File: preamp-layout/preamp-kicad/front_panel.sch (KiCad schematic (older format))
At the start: 11 parts

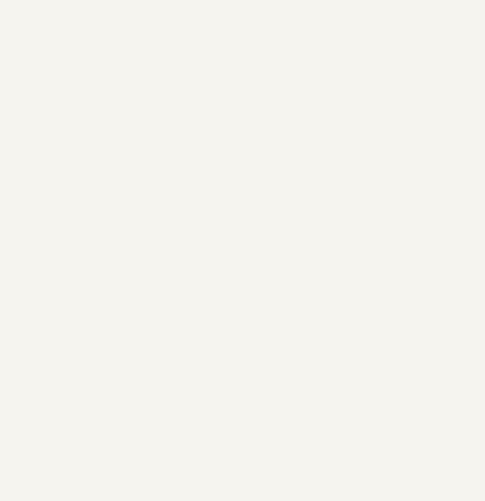
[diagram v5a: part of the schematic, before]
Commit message: Updates
Minor Readme updates.
Schematic:
 - Bus connector lines replaced single wire connectors
 - Title block populated.
 - Power Supply updates.
 - Preliminary Front Panel.
 - Minor MCU work.
 -
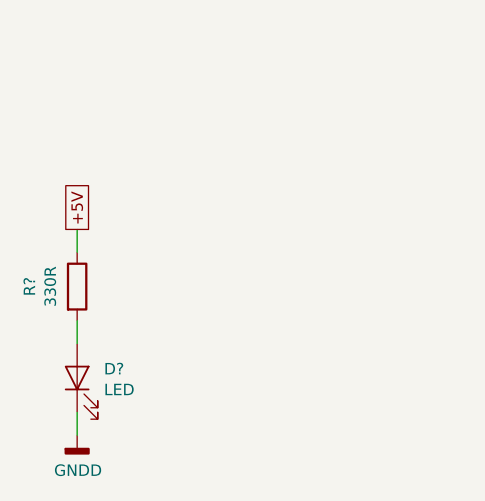
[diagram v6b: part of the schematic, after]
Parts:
- added D?: LED, symbol Device:LED
- added R?: 330R, symbol Device:R
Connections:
- net +5V: now also R?.1
- net GNDD: now also D?.1 (K)
- new net: D?.2 (A), R?.2
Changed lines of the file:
@@
 $Descr A4 11693 8268
 encoding utf-8
-Sheet 9 13
-Title ""
-Date ""
-Rev ""
+Sheet 7 13
+Title "Front Panel"
+Date "2020-01-09"
+Rev "A00"
 Comp ""
-Comment1 ""
-Comment2 ""
-Comment3 ""
-Comment4 ""
+Comment1 "creativecommons.org/licenses/by/4.0/"
+Comment2 "License: CC BY 4.0"
+Comment3 "github.com/SlurpyTurts/preamp"
+Comment4 "Author: Jordon Gerber"
 $EndDescr
 Text GLabel 5150 2250 1    50   UnSpc ~ 0
@@
 Wire Wire Line
 	1700 2100 1800 2100
+Text GLabel 1250 6200 1    50   UnSpc ~ 0
++5V
+$Comp
+L power:GNDD #PWR?
+U 1 1 5FF4C386
+P 1250 7100
+AR Path="/5E2D8DA2/5FF4C386" Ref="#PWR?"  Part="1"
+AR Path="/5E5ECAAE/5FF4C386" Ref="#PWR?"  Part="1"
+F 0 "#PWR?" H 1250 6850 50  0001 C CNN
+F 1 "GNDD" H 1254 6945 50  0000 C CNN
+F 2 "" H 1250 7100 50  0001 C CNN
+F 3 "" H 1250 7100 50  0001 C CNN
+	1    1250 7100
+	1    0    0    -1
+$EndComp
+$Comp
+L Device:R R?
+U 1 1 5FF4C38C
+P 1250 6450
+AR Path="/5E2D8DA2/5FF4C38C" Ref="R?"  Part="1"
+AR Path="/5FF4C38C" Ref="R?"  Part="1"
+AR Path="/5E5ECAAE/5FF4C38C" Ref="R?"  Part="1"
+F 0 "R?" V 1043 6450 50  0000 C CNN
+F 1 "330R" V 1134 6450 50  0000 C CNN
+F 2 "" V 1180 6450 50  0001 C CNN
+F 3 "~" H 1250 6450 50  0001 C CNN
+	1    1250 6450
+	1    0    0    -1
+$EndComp
+$Comp
+L Device:LED D?
+U 1 1 5FF4C392
+P 1250 6850
+AR Path="/5E2D8DA2/5FF4C392" Ref="D?"  Part="1"
+AR Path="/5E5ECAAE/5FF4C392" Ref="D?"  Part="1"
+F 0 "D?" V 1289 6733 50  0000 R CNN
+F 1 "LED" V 1198 6733 50  0000 R CNN
+F 2 "" H 1250 6850 50  0001 C CNN
+F 3 "~" H 1250 6850 50  0001 C CNN
+	1    1250 6850
+	0    -1   -1   0
+$EndComp
+Wire Wire Line
+	1250 6200 1250 6300
+Wire Wire Line
+	1250 6600 1250 6700
+Wire Wire Line
+	1250 7000 1250 7100
 $EndSCHEMATC

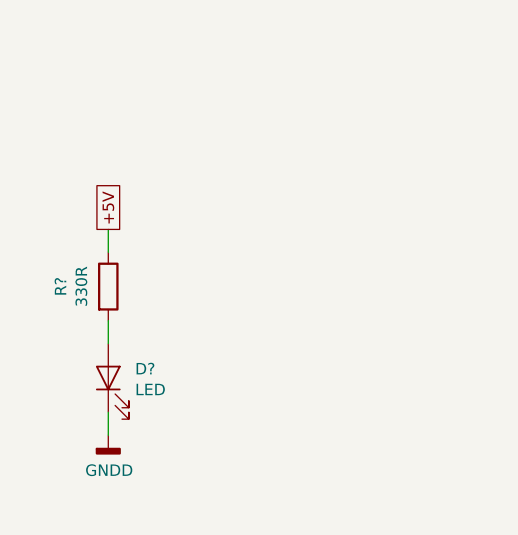
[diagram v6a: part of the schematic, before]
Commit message: Power conn cleanup
5V and 15V cleaned up on all sheets
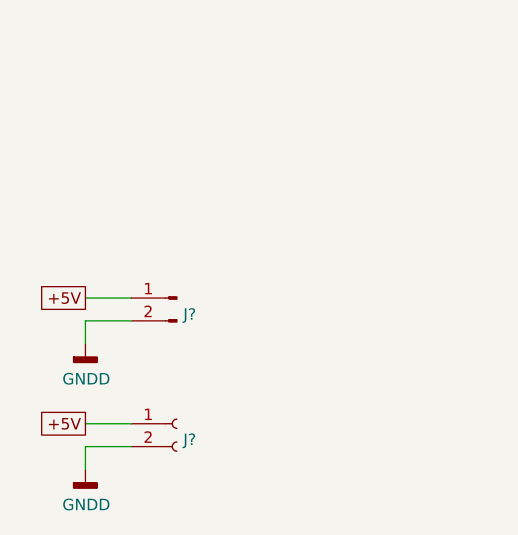
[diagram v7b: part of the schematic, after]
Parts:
- removed D?: LED, symbol Device:LED
- removed R?: 330R, symbol Device:R
- added J?: Conn_01x02_Male, symbol Connector:Conn_01x02_Male
- added J?: Conn_01x02_Female, symbol Connector:Conn_01x02_Female
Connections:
- net +5V: now also J?.1 (Pin_1), J?.1 (Pin_1)
- net GNDD: now also J?.2 (Pin_2), J?.2 (Pin_2)
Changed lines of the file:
@@
 $Descr A4 11693 8268
 encoding utf-8
-Sheet 7 13
+Sheet 6 13
 Title "Front Panel"
 Date "2020-01-09"
@@
 Wire Wire Line
 	1700 2100 1800 2100
-Text GLabel 1250 6200 1    50   UnSpc ~ 0
-+5V
-$Comp
-L power:GNDD #PWR?
-U 1 1 5FF4C386
-P 1250 7100
-AR Path="/5E2D8DA2/5FF4C386" Ref="#PWR?"  Part="1"
-AR Path="/5E5ECAAE/5FF4C386" Ref="#PWR?"  Part="1"
-F 0 "#PWR?" H 1250 6850 50  0001 C CNN
-F 1 "GNDD" H 1254 6945 50  0000 C CNN
-F 2 "" H 1250 7100 50  0001 C CNN
-F 3 "" H 1250 7100 50  0001 C CNN
-	1    1250 7100
-	1    0    0    -1
-$EndComp
-$Comp
-L Device:R R?
-U 1 1 5FF4C38C
-P 1250 6450
-AR Path="/5E2D8DA2/5FF4C38C" Ref="R?"  Part="1"
-AR Path="/5FF4C38C" Ref="R?"  Part="1"
-AR Path="/5E5ECAAE/5FF4C38C" Ref="R?"  Part="1"
-F 0 "R?" V 1043 6450 50  0000 C CNN
-F 1 "330R" V 1134 6450 50  0000 C CNN
-F 2 "" V 1180 6450 50  0001 C CNN
-F 3 "~" H 1250 6450 50  0001 C CNN
-	1    1250 6450
-	1    0    0    -1
-$EndComp
-$Comp
-L Device:LED D?
-U 1 1 5FF4C392
-P 1250 6850
-AR Path="/5E2D8DA2/5FF4C392" Ref="D?"  Part="1"
-AR Path="/5E5ECAAE/5FF4C392" Ref="D?"  Part="1"
-F 0 "D?" V 1289 6733 50  0000 R CNN
-F 1 "LED" V 1198 6733 50  0000 R CNN
-F 2 "" H 1250 6850 50  0001 C CNN
-F 3 "~" H 1250 6850 50  0001 C CNN
-	1    1250 6850
-	0    -1   -1   0
-$EndComp
-Wire Wire Line
-	1250 6200 1250 6300
-Wire Wire Line
-	1250 6600 1250 6700
-Wire Wire Line
-	1250 7000 1250 7100
+$Comp
+L Connector:Conn_01x02_Male J?
+U 1 1 60B80487
+P 1550 6500
+AR Path="/5E5EF2D4/60B80487" Ref="J?"  Part="1"
+AR Path="/6009D432/60B80487" Ref="J?"  Part="1"
+F 0 "J?" H 1522 6428 50  0000 R CNN
+F 1 "Conn_01x02_Male" H 1522 6383 50  0001 R CNN
+F 2 "" H 1550 6500 50  0001 C CNN
+F 3 "~" H 1550 6500 50  0001 C CNN
+	1    1550 6500
+	-1   0    0    -1
+$EndComp
+Text GLabel 1150 6500 0    50   UnSpc ~ 0
++5V
+$Comp
+L power:GNDD #PWR?
+U 1 1 60B8048E
+P 1150 6700
+AR Path="/5E5EF2D4/60B8048E" Ref="#PWR?"  Part="1"
+AR Path="/6009D432/60B8048E" Ref="#PWR?"  Part="1"
+F 0 "#PWR?" H 1150 6450 50  0001 C CNN
+F 1 "GNDD" H 1154 6545 50  0000 C CNN
+F 2 "" H 1150 6700 50  0001 C CNN
+F 3 "" H 1150 6700 50  0001 C CNN
+	1    1150 6700
+	1    0    0    -1
+$EndComp
+Wire Wire Line
+	1350 6600 1150 6600
+Wire Wire Line
+	1150 6600 1150 6700
+Wire Wire Line
+	1350 6500 1150 6500
+Text GLabel 1150 7050 0    50   UnSpc ~ 0
++5V
+$Comp
+L power:GNDD #PWR?
+U 1 1 60B80498
+P 1150 7250
+AR Path="/5E5EF2D4/60B80498" Ref="#PWR?"  Part="1"
+AR Path="/6009D432/60B80498" Ref="#PWR?"  Part="1"
+F 0 "#PWR?" H 1150 7000 50  0001 C CNN
+F 1 "GNDD" H 1154 7095 50  0000 C CNN
+F 2 "" H 1150 7250 50  0001 C CNN
+F 3 "" H 1150 7250 50  0001 C CNN
+	1    1150 7250
+	1    0    0    -1
+$EndComp
+Wire Wire Line
+	1350 7150 1150 7150
+Wire Wire Line
+	1150 7150 1150 7250
+Wire Wire Line
+	1350 7050 1150 7050
+$Comp
+L Connector:Conn_01x02_Female J?
+U 1 1 60B804B3
+P 1550 7050
+F 0 "J?" H 1578 6980 50  0000 L CNN
+F 1 "Conn_01x02_Female" H 1578 6935 50  0001 L CNN
+F 2 "" H 1550 7050 50  0001 C CNN
+F 3 "~" H 1550 7050 50  0001 C CNN
+	1    1550 7050
+	1    0    0    -1
+$EndComp
 $EndSCHEMATC
